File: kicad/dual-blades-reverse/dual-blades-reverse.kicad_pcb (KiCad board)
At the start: 2 copper layers, 138.1 x 93.6 mm, 56 parts, among them J1 nice_view, J2 JST, SW1 SW_Push, SW10 SW_Push, SW11 SW_Push, SW12 SW_Push, SW13 SW_Push, SW14 SW_Push, SW15 SW_Push, SW16 SW_Push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

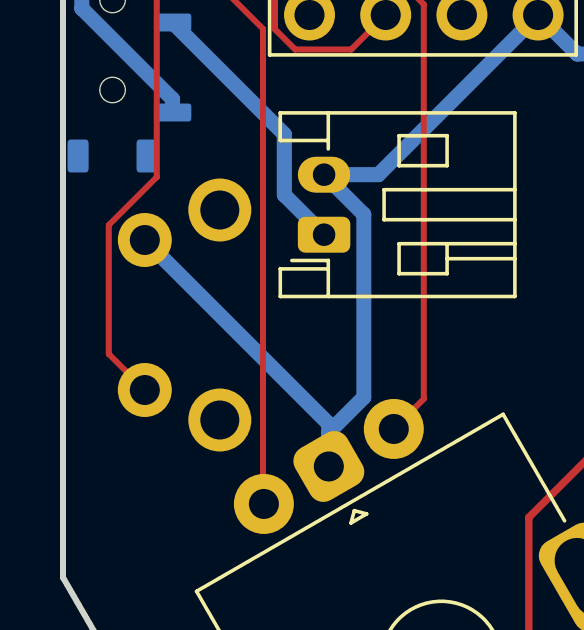
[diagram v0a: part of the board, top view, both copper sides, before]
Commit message: update pcb gerbers and add keyboard image
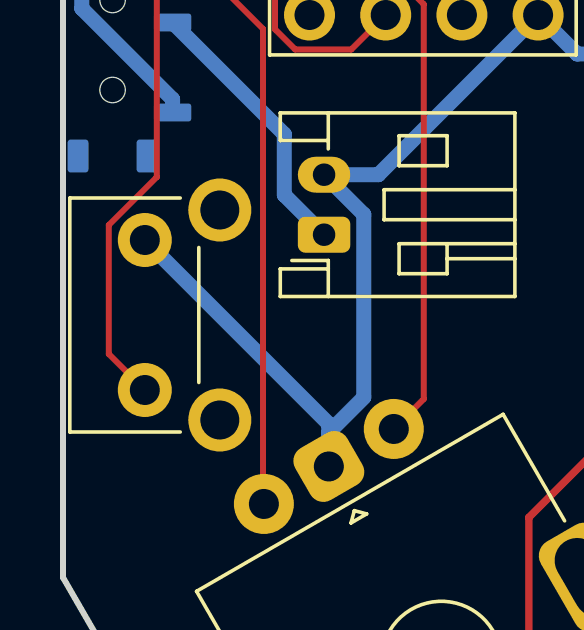
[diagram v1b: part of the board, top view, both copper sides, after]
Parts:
- SW24: moved to F.Cu
- turned SW24 to 90 degrees
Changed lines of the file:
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@@
     (pad "" np_thru_hole circle locked (at 0 0) (size 4.3 4.3) (drill 4.3) (layers "*.Cu" "*.Mask"))
+  )
+  (footprint "marbastlib-various:SW_SKHLLCA010" locked (layer "F.Cu")
+    (at 83.74965 108.1768 90)
+    (descr "alps SKHLLCA010 DIP pushbutton")
+    (tags "alps tht dip pushbutton SPST")
+    (property "Sheetfile" "dual-blades.kicad_sch")
+    (property "Sheetname" "")
+    (property "ki_description" "Push button switch, generic, two pins")
+    (property "ki_keywords" "switch normally-open pushbutton push-button")
+    (attr through_hole)
+    (fp_text reference "SW24" (at -2.25 3.5 90 unlocked) (layer "F.SilkS") hide
+        (effects (font (size 1 1) (thickness 0.15)))
+    )
+    (fp_text value "SW_SKHLLCA010" (at 0 1.55 90 unlocked) (layer "F.Fab")
+        (effects (font (size 1 1) (thickness 0.15)))
+    )
+    (fp_text user "${REFERENCE}" (at 0 -1.45 90) (layer "F.Fab")
+        (effects (font (size 1 1) (thickness 0.15)))
+    )
+    (fp_line (start -3.9 -3.75) (end 3.9 -3.75)
+      (stroke (width 0.12) (type solid)) (layer "F.SilkS"))
+    (fp_line (start -3.9 -0.07) (end -3.9 -3.75)
+      (stroke (width 0.12) (type solid)) (layer "F.SilkS"))
+    (fp_line (start -2.25 0.55) (end 2.25 0.55)
+      (stroke (width 0.12) (type solid)) (layer "F.SilkS"))
+    (fp_line (start 3.9 -0.07) (end 3.9 -3.75)
+      (stroke (width 0.12) (type solid)) (layer "F.SilkS"))
+    (fp_line (start -1.25 -5) (end 1.25 -5)
+      (stroke (width 0.12) (type solid)) (layer "Dwgs.User"))
+    (fp_line (start -1.25 -3.75) (end -1.25 -5)
+      (stroke (width 0.12) (type solid)) (layer "Dwgs.User"))
+    (fp_line (start 1.25 -3.75) (end 1.25 -5)
+      (stroke (width 0.12) (type solid)) (layer "Dwgs.User"))
+    (fp_line (start -3.65 -4.97) (end -3.65 2.18)
+      (stroke (width 0.05) (type solid)) (layer "F.CrtYd"))
+    (fp_line (start -3.65 -4.97) (end 3.65 -4.97)
+      (stroke (width 0.05) (type solid)) (layer "F.CrtYd"))
+    (fp_line (start -3.65 2.18) (end 3.65 2.18)
+      (stroke (width 0.05) (type solid)) (layer "F.CrtYd"))
+    (fp_line (start 3.65 -4.97) (end 3.65 2.18)
+      (stroke (width 0.05) (type solid)) (layer "F.CrtYd"))
+    (fp_line (start -3.9 -3.75) (end 3.9 -3.75)
+      (stroke (width 0.12) (type solid)) (layer "F.Fab"))
+    (fp_line (start -3.9 0.55) (end -3.9 -3.75)
+      (stroke (width 0.12) (type solid)) (layer "F.Fab"))
+    (fp_line (start -3.9 0.55) (end 3.9 0.55)
+      (stroke (width 0.12) (type solid)) (layer "F.Fab"))
+    (fp_line (start -1.25 -5) (end 1.25 -5)
+      (stroke (width 0.12) (type solid)) (layer "F.Fab"))
+    (fp_line (start -1.25 -3.75) (end -1.25 -5)
+      (stroke (width 0.12) (type solid)) (layer "F.Fab"))
+    (fp_line (start 1.25 -3.75) (end 1.25 -5)
+      (stroke (width 0.12) (type solid)) (layer "F.Fab"))
+    (fp_line (start 3.9 0.55) (end 3.9 -3.75)
+      (stroke (width 0.12) (type solid)) (layer "F.Fab"))
+    (pad "1" thru_hole circle locked (at 2.5 -1.25 90) (size 1.8 1.8) (drill 1) (layers "*.Cu" "B.Mask")
+      (net 42 "RST") (pinfunction "1") (pintype "passive"))
+    (pad "2" thru_hole circle locked (at -2.5 -1.25 90) (size 1.8 1.8) (drill 1) (layers "*.Cu" "B.Mask")
+      (net 29 "GND") (pinfunction "2") (pintype "passive"))
+    (pad "MP" thru_hole circle locked (at -3.5 1.25 90) (size 2.1 2.1) (drill 1.3) (layers "*.Cu" "*.Mask"))
+    (pad "MP" thru_hole circle locked (at 3.5 1.25 90) (size 2.1 2.1) (drill 1.3) (layers "*.Cu" "*.Mask"))
+    (model "${KIPRJMOD}/libs/ebastler/marbastlib/3dmodels/SW_SKHLLC.step"
+      (offset (xyz 0 3.25 2.5))
+      (scale (xyz 1 1 1))
+      (rotate (xyz -90 0 180))
+    )
   )
   (footprint "Diode_THT:D_DO-35_SOD27_P7.62mm_Horizontal" locked (layer "F.Cu")
@@
     )
   )
-  (footprint "marbastlib-various:SW_SKHLLCA010" locked (layer "B.Cu")
-    (at 83.74965 108.1768 -90)
-    (descr "alps SKHLLCA010 DIP pushbutton")
-    (tags "alps tht dip pushbutton SPST")
-    (property "Sheetfile" "dual-blades.kicad_sch")
-    (property "Sheetname" "")
-    (property "ki_description" "Push button switch, generic, two pins")
-    (property "ki_keywords" "switch normally-open pushbutton push-button")
-    (attr through_hole)
-    (fp_text reference "SW24" (at -2.25 -3.5 90 unlocked) (layer "B.SilkS") hide
-        (effects (font (size 1 1) (thickness 0.15)) (justify mirror))
-    )
-    (fp_text value "SW_SKHLLCA010" (at 0 -1.55 90 unlocked) (layer "B.Fab")
-        (effects (font (size 1 1) (thickness 0.15)) (justify mirror))
-    )
-    (fp_text user "${REFERENCE}" (at 0 1.45 90) (layer "B.Fab")
-        (effects (font (size 1 1) (thickness 0.15)) (justify mirror))
-    )
-    (fp_line (start -3.9 0.07) (end -3.9 3.75)
-      (stroke (width 0.12) (type solid)) (layer "B.SilkS"))
-    (fp_line (start -3.9 3.75) (end 3.9 3.75)
-      (stroke (width 0.12) (type solid)) (layer "B.SilkS"))
-    (fp_line (start -2.25 -0.55) (end 2.25 -0.55)
-      (stroke (width 0.12) (type solid)) (layer "B.SilkS"))
-    (fp_line (start 3.9 0.07) (end 3.9 3.75)
-      (stroke (width 0.12) (type solid)) (layer "B.SilkS"))
-    (fp_line (start -1.25 3.75) (end -1.25 5)
-      (stroke (width 0.12) (type solid)) (layer "Dwgs.User"))
-    (fp_line (start -1.25 5) (end 1.25 5)
-      (stroke (width 0.12) (type solid)) (layer "Dwgs.User"))
-    (fp_line (start 1.25 3.75) (end 1.25 5)
-      (stroke (width 0.12) (type solid)) (layer "Dwgs.User"))
-    (fp_line (start -3.65 -2.18) (end 3.65 -2.18)
-      (stroke (width 0.05) (type solid)) (layer "B.CrtYd"))
-    (fp_line (start -3.65 4.97) (end -3.65 -2.18)
-      (stroke (width 0.05) (type solid)) (layer "B.CrtYd"))
-    (fp_line (start -3.65 4.97) (end 3.65 4.97)
-      (stroke (width 0.05) (type solid)) (layer "B.CrtYd"))
-    (fp_line (start 3.65 4.97) (end 3.65 -2.18)
-      (stroke (width 0.05) (type solid)) (layer "B.CrtYd"))
-    (fp_line (start -3.9 -0.55) (end -3.9 3.75)
-      (stroke (width 0.12) (type solid)) (layer "B.Fab"))
-    (fp_line (start -3.9 -0.55) (end 3.9 -0.55)
-      (stroke (width 0.12) (type solid)) (layer "B.Fab"))
-    (fp_line (start -3.9 3.75) (end 3.9 3.75)
-      (stroke (width 0.12) (type solid)) (layer "B.Fab"))
-    (fp_line (start -1.25 3.75) (end -1.25 5)
-      (stroke (width 0.12) (type solid)) (layer "B.Fab"))
-    (fp_line (start -1.25 5) (end 1.25 5)
-      (stroke (width 0.12) (type solid)) (layer "B.Fab"))
-    (fp_line (start 1.25 3.75) (end 1.25 5)
-      (stroke (width 0.12) (type solid)) (layer "B.Fab"))
-    (fp_line (start 3.9 -0.55) (end 3.9 3.75)
-      (stroke (width 0.12) (type solid)) (layer "B.Fab"))
-    (pad "1" thru_hole circle locked (at 2.5 1.25 270) (size 1.8 1.8) (drill 1) (layers "*.Cu" "F.Mask")
-      (net 42 "RST") (pinfunction "1") (pintype "passive"))
-    (pad "2" thru_hole circle locked (at -2.5 1.25 270) (size 1.8 1.8) (drill 1) (layers "*.Cu" "F.Mask")
-      (net 29 "GND") (pinfunction "2") (pintype "passive"))
-    (pad "MP" thru_hole circle locked (at -3.5 -1.25 270) (size 2.1 2.1) (drill 1.3) (layers "*.Cu" "*.Mask"))
-    (pad "MP" thru_hole circle locked (at 3.5 -1.25 270) (size 2.1 2.1) (drill 1.3) (layers "*.Cu" "*.Mask"))
-    (model "${KIPRJMOD}/libs/ebastler/marbastlib/3dmodels/SW_SKHLLC.step"
-      (offset (xyz 0 3.25 2.5))
-      (scale (xyz 1 1 1))
-      (rotate (xyz -90 0 180))
-    )
-  )
